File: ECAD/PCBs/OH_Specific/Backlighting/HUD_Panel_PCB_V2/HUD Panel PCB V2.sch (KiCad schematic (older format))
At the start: 58 parts, among them J1 Conn_01x04_Female, J2 Conn_01x04_Female

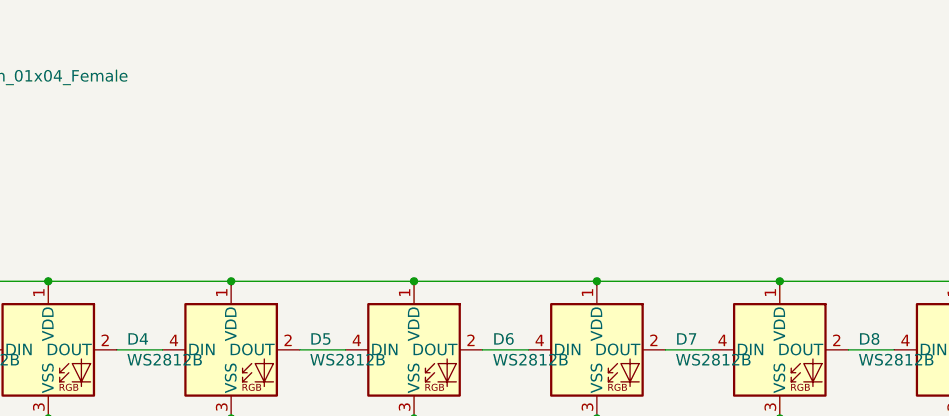
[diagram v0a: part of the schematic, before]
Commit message: HUD Panel Backlighting Update
The V2.0 board seems to have lost its silk screening and routing, that has been redone.
Changed - Location of the following LEDs to clear the pot mounting nut: D8, D9, D40, D41, D53, D54.
General manufacturing file cleanup into version folders.
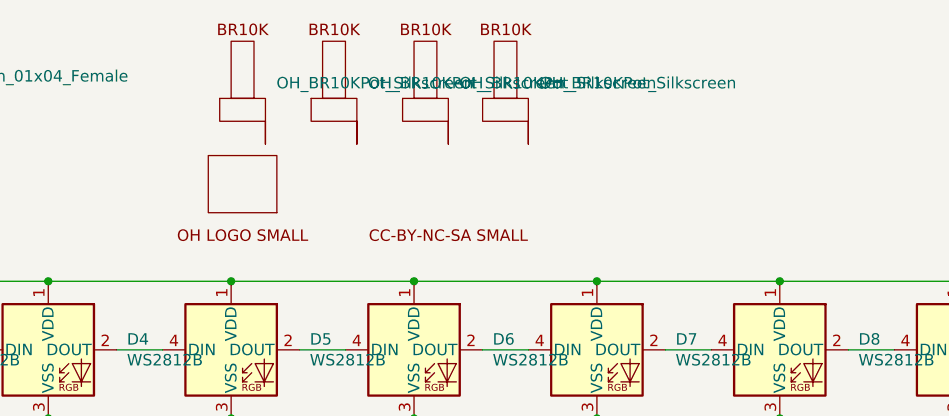
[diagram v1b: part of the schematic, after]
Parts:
- added LOGO1, LOGO3, LOGO4, LOGO6: OH_BR10KPot_Silkscreen, OH_Backlighting:BR10K_Pot_Silkscreen, symbol KiCadCustomLib:OH_BR10KPot_Silkscreen
- added LOGO2: OpenHornetLogoSmall, OH_KiCAD_Libraries:OH_LOGO_37.7mm_5.9mm, symbol KiCadCustomLib:OpenHornetLogoSmall
- added LOGO5: CC-BY-NC-SA_Icon, OH_KiCAD_Libraries:CC-BY-NC-SA-Small, symbol KiCadCustomLib:CC-BY-NC-SA_Icon
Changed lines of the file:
@@
 Text Label 3700 950  3    50   ~ 0
 DATAOUT
+$Comp
+L KiCadCustomLib:OH_BR10KPot_Silkscreen LOGO1
+U 1 1 61951C93
+P 5000 1100
+F 0 "LOGO1" H 5000 850 50  0001 C CNN
+F 1 "OH_BR10KPot_Silkscreen" H 5148 1267 50  0000 L CNN
+F 2 "OH_Backlighting:BR10K_Pot_Silkscreen" H 5050 750 50  0001 C CNN
+F 3 "" H 5050 850 50  0001 C CNN
+	1    5000 1100
+	1    0    0    -1
+$EndComp
+$Comp
+L KiCadCustomLib:OH_BR10KPot_Silkscreen LOGO3
+U 1 1 6195354C
+P 5400 1100
+F 0 "LOGO3" H 5400 850 50  0001 C CNN
+F 1 "OH_BR10KPot_Silkscreen" H 5548 1267 50  0000 L CNN
+F 2 "OH_Backlighting:BR10K_Pot_Silkscreen" H 5450 750 50  0001 C CNN
+F 3 "" H 5450 850 50  0001 C CNN
+	1    5400 1100
+	1    0    0    -1
+$EndComp
+$Comp
+L KiCadCustomLib:OH_BR10KPot_Silkscreen LOGO4
+U 1 1 61961811
+P 5800 1100
+F 0 "LOGO4" H 5800 850 50  0001 C CNN
+F 1 "OH_BR10KPot_Silkscreen" H 5948 1267 50  0000 L CNN
+F 2 "OH_Backlighting:BR10K_Pot_Silkscreen" H 5850 750 50  0001 C CNN
+F 3 "" H 5850 850 50  0001 C CNN
+	1    5800 1100
+	1    0    0    -1
+$EndComp
+$Comp
+L KiCadCustomLib:OH_BR10KPot_Silkscreen LOGO6
+U 1 1 6196F889
+P 6150 1100
+F 0 "LOGO6" H 6150 850 50  0001 C CNN
+F 1 "OH_BR10KPot_Silkscreen" H 6298 1267 50  0000 L CNN
+F 2 "OH_Backlighting:BR10K_Pot_Silkscreen" H 6200 750 50  0001 C CNN
+F 3 "" H 6200 850 50  0001 C CNN
+	1    6150 1100
+	1    0    0    -1
+$EndComp
+$Comp
+L KiCadCustomLib:OpenHornetLogoSmall LOGO2
+U 1 1 6197F3AC
+P 5000 1700
+F 0 "LOGO2" H 5000 1700 50  0001 C CNN
+F 1 "OpenHornetLogoSmall" H 5000 1700 50  0001 C CNN
+F 2 "OH_KiCAD_Libraries:OH_LOGO_37.7mm_5.9mm" H 5000 1700 50  0001 C CNN
+F 3 "" H 5000 1700 50  0001 C CNN
+	1    5000 1700
+	1    0    0    -1
+$EndComp
+$Comp
+L KiCadCustomLib:CC-BY-NC-SA_Icon LOGO5
+U 1 1 61980D84
+P 5850 1700
+F 0 "LOGO5" H 5850 1700 50  0001 C CNN
+F 1 "CC-BY-NC-SA_Icon" H 5850 1700 50  0001 C CNN
+F 2 "OH_KiCAD_Libraries:CC-BY-NC-SA-Small" H 5850 1700 50  0001 C CNN
+F 3 "" H 5850 1700 50  0001 C CNN
+	1    5850 1700
+	1    0    0    -1
+$EndComp
 $EndSCHEMATC
